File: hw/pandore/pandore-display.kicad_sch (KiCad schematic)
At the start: 26 parts, among them J1 HDMI, Q1 MOSFET_EN-N, Q2 MOSFET_EN-N, Q3 MOSFET_EN-N, Q4 MOSFET_EN-N

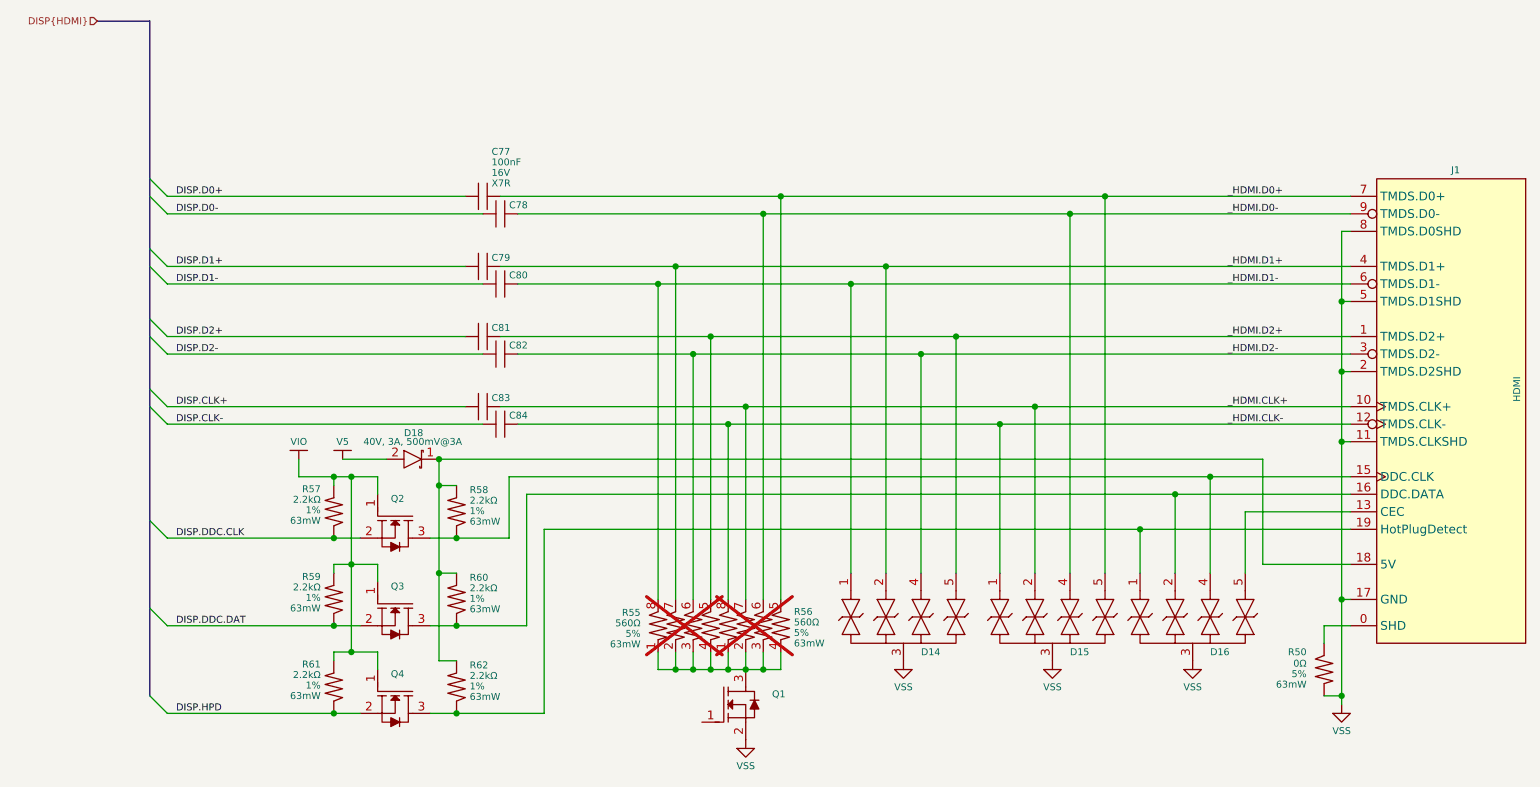
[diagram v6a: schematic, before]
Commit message: finished adding mpn,mfg to all parts, finished routing placement
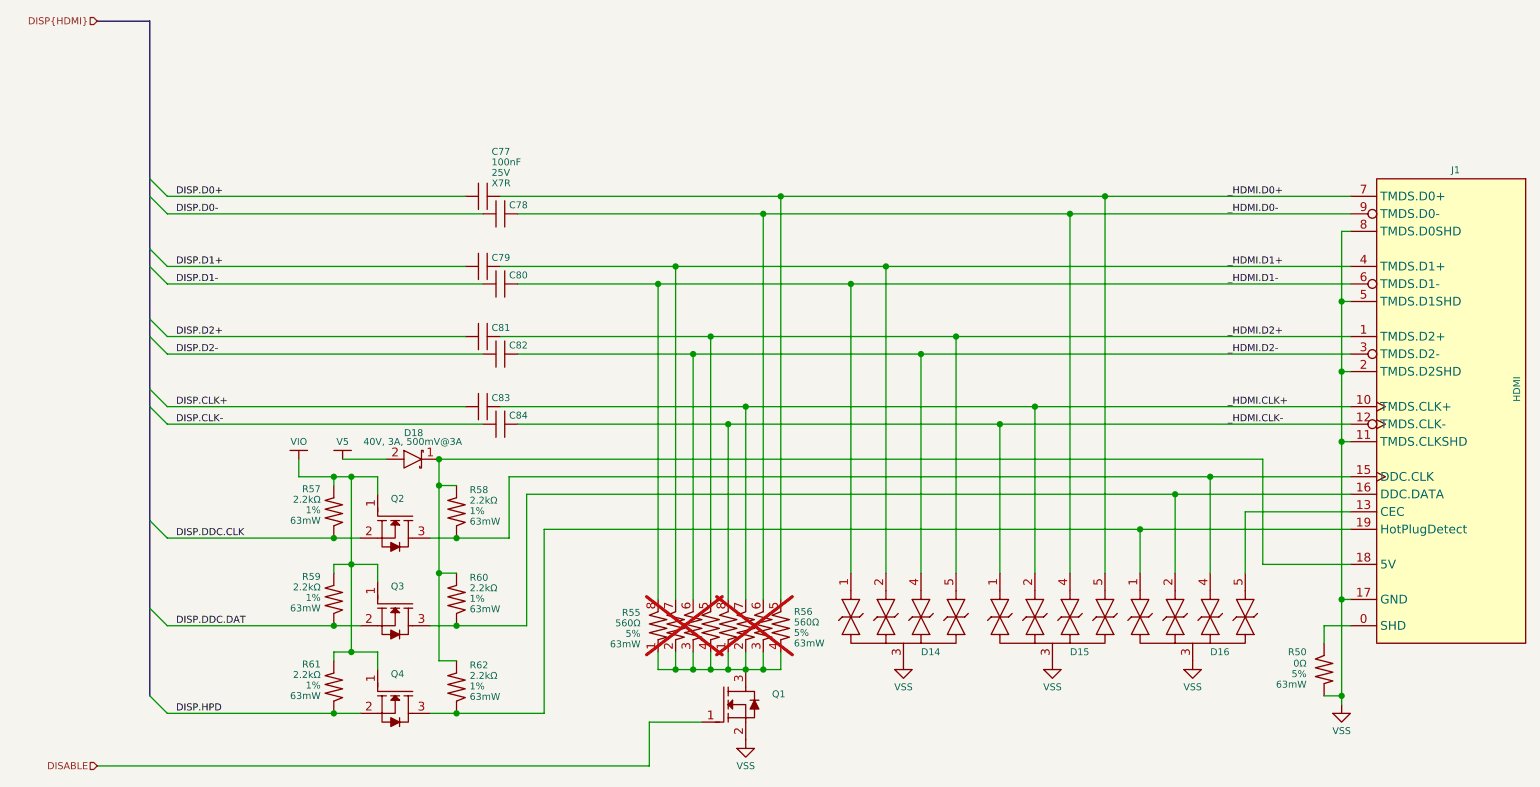
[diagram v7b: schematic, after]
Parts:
- C77, C78, C79, C80, C81, C82, C83, C84: MFG2 Samsung Electro-Mechanics -> (none); MFG3 Taiyo Yuden -> (none); MPN2 CL05B104KA5NNNC -> (none); MPN3 EMK105B7104KV-F -> (none); Voltage 16V -> 25V
- R50: Link (none) -> https://yageogroup.com/products/Resistors/part/RC0402JR-070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; MFG (none) -> Yageo; MFG2 (none) -> Stackpole; MFG3 (none) -> Vishay Dale; MPN (none) -> RC0402JR-070RL; MPN2 (none) -> RMCF0402ZT0R00; MPN3 (none) -> CRCW04020000Z0ED
- R57, R58, R59, R60, R61, R62: Link (none) -> https://yageogroup.com/products/Resistors/part/RC0402FR-072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; MFG (none) -> YAGEO; MPN (none) -> RC0402FR-072K2L
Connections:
- net DISABLE: now reaches Q1.1 (G)
